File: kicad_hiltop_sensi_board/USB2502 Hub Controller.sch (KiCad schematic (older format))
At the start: 39 parts, among them U27 USB2502, U7 AT24C02C-SSHM-T, Y1 50ppm 24.000MHZ

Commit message: Updated LBBC board and Board layout started
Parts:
- JP14: footprint (none) -> Connector_PinHeader_1.00mm:PinHeader_1x02_P1.00mm_Vertical
- L1: footprint (none) -> Inductor_SMD:L_0805_2012Metric
- U7: footprint (none) -> Package_SO:SOIC-8_3.9x4.9mm_P1.27mm
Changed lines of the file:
@@
 F 0 "JP14" V 2696 8612 50  0000 R CNN
 F 1 "DNF" V 2605 8612 50  0000 R CNN
-F 2 "" H 2650 8700 50  0001 C CNN
+F 2 "Connector_PinHeader_1.00mm:PinHeader_1x02_P1.00mm_Vertical" H 2650 8700 50  0001 C CNN
 F 3 "" H 2650 8700 50  0001 C CNN
 	1    2650 8700
@@
 F 0 "L1" V 7500 8450 50  0000 C CNN
 F 1 "FB 500mA/0.10DCR" V 7600 8800 50  0000 C CNN
-F 2 "" V 7680 8700 50  0001 C CNN
+F 2 "Inductor_SMD:L_0805_2012Metric" V 7680 8700 50  0001 C CNN
 F 3 "" H 7750 8700 50  0001 C CNN
 	1    7750 8700
@@
 F 0 "U7" H 9375 6187 60  0000 C CNN
 F 1 "AT24C02C-SSHM-T" H 9375 6081 60  0000 C CNN
-F 2 "" H 9300 5150 60  0001 C CNN
+F 2 "Package_SO:SOIC-8_3.9x4.9mm_P1.27mm" H 9300 5150 60  0001 C CNN
 F 3 "" H 9300 5150 60  0001 C CNN
 	1    9350 5700

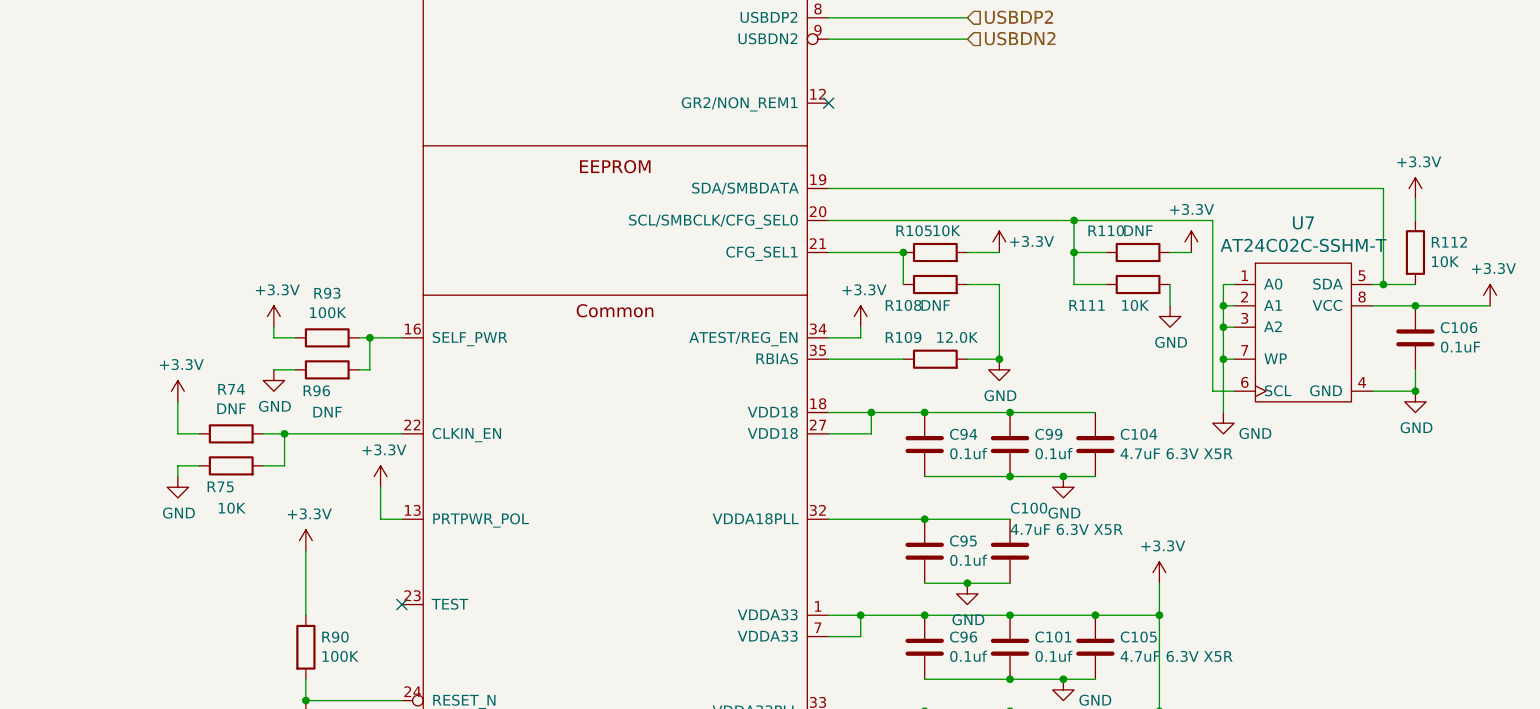
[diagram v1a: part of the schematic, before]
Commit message: Updated board layout LBBC sensi board
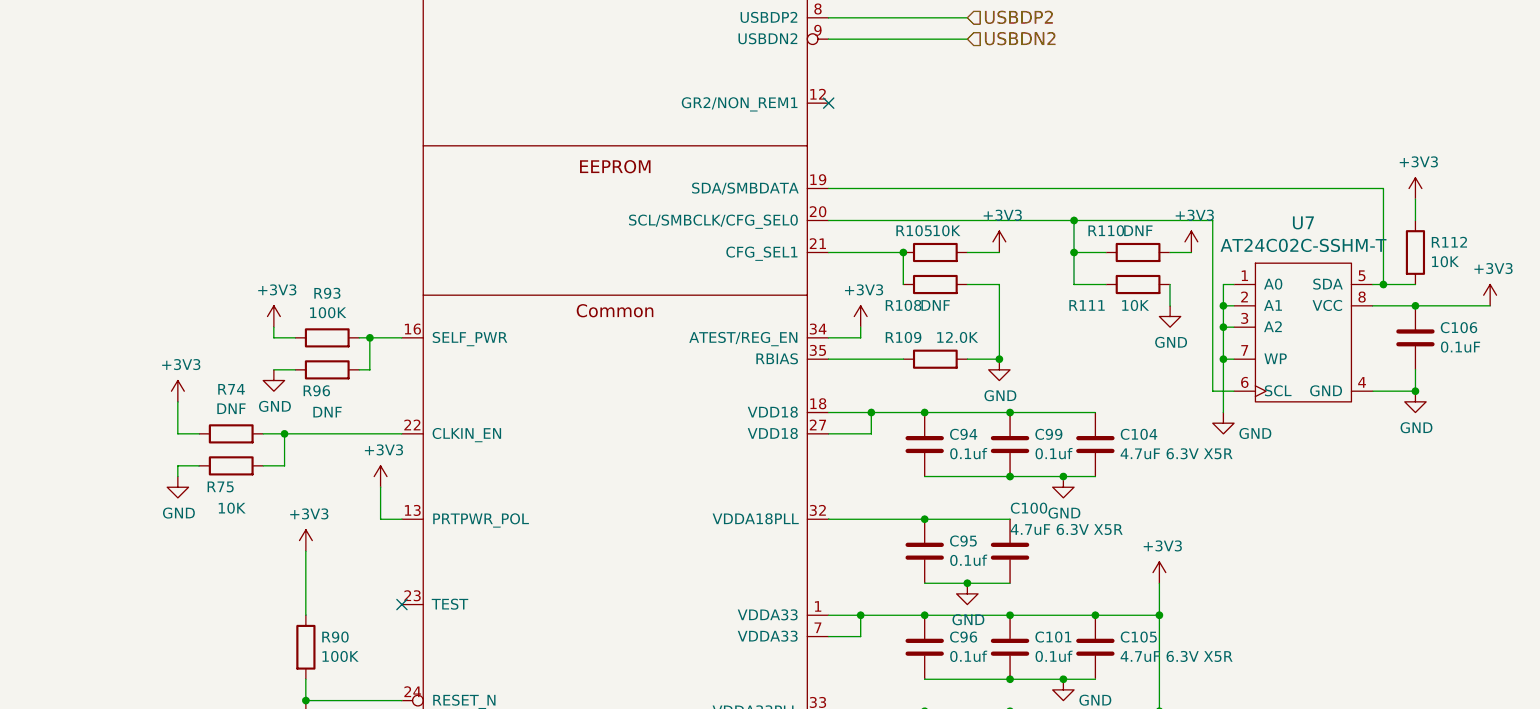
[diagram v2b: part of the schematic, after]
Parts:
- D1: footprint (none) -> Diode_SMD:D_SMA
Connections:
- net +5V_ISO1 renamed +3V3
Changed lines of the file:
@@
 Connection ~ 8000 7500
 Connection ~ 8400 7050
-$Comp
-L Devtank:+3.3V #PWR0178
-U 1 1 5D9260A5
-P 8700 6900
-F 0 "#PWR0178" H 8700 6750 50  0001 C CNN
-F 1 "+3.3V" H 8715 7073 50  0000 C CNN
-F 2 "" H 8700 6900 50  0000 C CNN
-F 3 "" H 8700 6900 50  0000 C CNN
-	1    8700 6900
-	1    0    0    -1
-$EndComp
 Wire Wire Line
 	8700 7050 8700 6900
@@
 	1    0    0    -1
 $EndComp
-$Comp
-L Devtank:+3.3V #PWR0201
-U 1 1 5D96A9AB
-P 7300 5700
-F 0 "#PWR0201" H 7300 5550 50  0001 C CNN
-F 1 "+3.3V" H 7315 5873 50  0000 C CNN
-F 2 "" H 7300 5700 50  0000 C CNN
-F 3 "" H 7300 5700 50  0000 C CNN
-	1    7300 5700
-	1    0    0    -1
-$EndComp
 Wire Wire Line
 	7300 5750 7300 5700
@@
 	7500 5500 7500 5350
 Connection ~ 7500 5350
-$Comp
-L Devtank:+3.3V #PWR0202
-U 1 1 5D97496E
-P 7950 5350
-F 0 "#PWR0202" H 7950 5200 50  0001 C CNN
-F 1 "+3.3V" H 8100 5400 50  0000 C CNN
-F 2 "" H 7950 5350 50  0000 C CNN
-F 3 "" H 7950 5350 50  0000 C CNN
-	1    7950 5350
-	1    0    0    -1
-$EndComp
 Wire Wire Line
 	7800 5350 7950 5350
@@
 	8300 5500 8300 5350
 Connection ~ 8300 5350
-$Comp
-L Devtank:+3.3V #PWR0205
-U 1 1 5D991A44
-P 8850 5350
-F 0 "#PWR0205" H 8850 5200 50  0001 C CNN
-F 1 "+3.3V" H 8850 5550 50  0000 C CNN
-F 2 "" H 8850 5350 50  0000 C CNN
-F 3 "" H 8850 5350 50  0000 C CNN
-	1    8850 5350
-	1    0    0    -1
-$EndComp
 Wire Wire Line
 	8750 5350 8850 5350
@@
 Wire Wire Line
 	9900 6000 9700 6000
-$Comp
-L Devtank:+3.3V #PWR0209
-U 1 1 5D9B0D62
-P 9900 5100
-F 0 "#PWR0209" H 9900 4950 50  0001 C CNN
-F 1 "+3.3V" H 9915 5273 50  0000 C CNN
-F 2 "" H 9900 5100 50  0000 C CNN
-F 3 "" H 9900 5100 50  0000 C CNN
-	1    9900 5100
-	1    0    0    -1
-$EndComp
 $Comp
 L device:R R112
@@
 Wire Wire Line
 	4700 7900 4700 7750
-$Comp
-L Devtank:+3.3V #PWR0211
-U 1 1 5DAA965D
-P 4700 6750
-F 0 "#PWR0211" H 4700 6600 50  0001 C CNN
-F 1 "+3.3V" H 4715 6923 50  0000 C CNN
-F 2 "" H 4700 6750 50  0000 C CNN
-F 3 "" H 4700 6750 50  0000 C CNN
-	1    4700 6750
-	1    0    0    -1
-$EndComp
 Wire Wire Line
 	4500 6200 4600 6200
@@
 	4600 6200 5150 6200
 Connection ~ 4600 6200
-$Comp
-L Devtank:+3.3V #PWR0212
-U 1 1 5DAE308D
-P 4100 6050
-F 0 "#PWR0212" H 4100 5900 50  0001 C CNN
-F 1 "+3.3V" H 4115 6223 50  0000 C CNN
-F 2 "" H 4100 6050 50  0000 C CNN
-F 3 "" H 4100 6050 50  0000 C CNN
-	1    4100 6050
-	1    0    0    -1
-$EndComp
 $Comp
 L power:GND #PWR0213
@@
 Wire Wire Line
 	4650 5900 4550 5900
-$Comp
-L Devtank:+3.3V #PWR0215
-U 1 1 5DB51EA9
-P 4550 5700
-F 0 "#PWR0215" H 4550 5550 50  0001 C CNN
-F 1 "+3.3V" H 4565 5873 50  0000 C CNN
-F 2 "" H 4550 5700 50  0000 C CNN
-F 3 "" H 4550 5700 50  0000 C CNN
-	1    4550 5700
-	1    0    0    -1
-$EndComp
 Wire Wire Line
 	4650 5750 4550 5750
@@
 Wire Wire Line
 	9900 5100 9900 5200
-$Comp
-L Devtank:+3.3V #PWR0223
-U 1 1 5DC7B6F6
-P 10250 5600
-F 0 "#PWR0223" H 10250 5450 50  0001 C CNN
-F 1 "+3.3V" H 10265 5773 50  0000 C CNN
-F 2 "" H 10250 5600 50  0000 C CNN
-F 3 "" H 10250 5600 50  0000 C CNN
-	1    10250 5600
-	1    0    0    -1
-$EndComp
 Wire Wire Line
 	9900 5600 10250 5600
@@
 F 0 "D1" H 4650 2266 50  0000 C CNN
 F 1 "B240A-13" H 4650 2175 50  0000 C CNN
-F 2 "" H 4650 2050 50  0001 C CNN
+F 2 "Diode_SMD:D_SMA" H 4650 2050 50  0001 C CNN
 F 3 "" H 4650 2050 50  0001 C CNN
 	1    4650 2050
@@
 Wire Wire Line
 	4700 6750 4700 7050
-$Comp
-L Devtank:+3.3V #PWR04
-U 1 1 5DC261DE
-P 5050 6450
-F 0 "#PWR04" H 5050 6300 50  0001 C CNN
-F 1 "+3.3V" H 5065 6623 50  0000 C CNN
-F 2 "" H 5050 6450 50  0000 C CNN
-F 3 "" H 5050 6450 50  0000 C CNN
-	1    5050 6450
-	1    0    0    -1
-$EndComp
 Wire Wire Line
 	5150 6600 5050 6600
@@
 	1    0    0    -1
 $EndComp
+$Comp
+L power:+3V3 #PWR?
+U 1 1 5E653672
+P 8700 6900
+AR Path="/5E653672" Ref="#PWR?"  Part="1"
+AR Path="/5D8D08E6/5E653672" Ref="#PWR0178"  Part="1"
+F 0 "#PWR0178" H 8700 6750 50  0001 C CNN
+F 1 "+3V3" H 8715 7073 50  0000 C CNN
+F 2 "" H 8700 6900 50  0001 C CNN
+F 3 "" H 8700 6900 50  0001 C CNN
+	1    8700 6900
+	1    0    0    -1
+$EndComp
+$Comp
+L power:+3V3 #PWR?
+U 1 1 5E664207
+P 7300 5700
+AR Path="/5E664207" Ref="#PWR?"  Part="1"
+AR Path="/5D8D08E6/5E664207" Ref="#PWR0201"  Part="1"
+F 0 "#PWR0201" H 7300 5550 50  0001 C CNN
+F 1 "+3V3" H 7315 5873 50  0000 C CNN
+F 2 "" H 7300 5700 50  0001 C CNN
+F 3 "" H 7300 5700 50  0001 C CNN
+	1    7300 5700
+	1    0    0    -1
+$EndComp
+$Comp
+L power:+3V3 #PWR?
+U 1 1 5E674F93
+P 7950 5350
+AR Path="/5E674F93" Ref="#PWR?"  Part="1"
+AR Path="/5D8D08E6/5E674F93" Ref="#PWR0202"  Part="1"
+F 0 "#PWR0202" H 7950 5200 50  0001 C CNN
+F 1 "+3V3" H 7965 5523 50  0000 C CNN
+F 2 "" H 7950 5350 50  0001 C CNN
+F 3 "" H 7950 5350 50  0001 C CNN
+	1    7950 5350
+	1    0    0    -1
+$EndComp
+$Comp
+L power:+3V3 #PWR?
+U 1 1 5E685BFA
+P 8850 5350
+AR Path="/5E685BFA" Ref="#PWR?"  Part="1"
+AR Path="/5D8D08E6/5E685BFA" Ref="#PWR0205"  Part="1"
+F 0 "#PWR0205" H 8850 5200 50  0001 C CNN
+F 1 "+3V3" H 8865 5523 50  0000 C CNN
+F 2 "" H 8850 5350 50  0001 C CNN
+F 3 "" H 8850 5350 50  0001 C CNN
+	1    8850 5350
+	1    0    0    -1
+$EndComp
+$Comp
+L power:+3V3 #PWR?
+U 1 1 5E693D22
+P 9900 5100
+AR Path="/5E693D22" Ref="#PWR?"  Part="1"
+AR Path="/5D8D08E6/5E693D22" Ref="#PWR0209"  Part="1"
+F 0 "#PWR0209" H 9900 4950 50  0001 C CNN
+F 1 "+3V3" H 9915 5273 50  0000 C CNN
+F 2 "" H 9900 5100 50  0001 C CNN
+F 3 "" H 9900 5100 50  0001 C CNN
+	1    9900 5100
+	1    0    0    -1
+$EndComp
+$Comp
+L power:+3V3 #PWR?
+U 1 1 5E6A7C04
+P 4700 6750
+AR Path="/5E6A7C04" Ref="#PWR?"  Part="1"
+AR Path="/5D8D08E6/5E6A7C04" Ref="#PWR0211"  Part="1"
+F 0 "#PWR0211" H 4700 6600 50  0001 C CNN
+F 1 "+3V3" H 4715 6923 50  0000 C CNN
+F 2 "" H 4700 6750 50  0001 C CNN
+F 3 "" H 4700 6750 50  0001 C CNN
+	1    4700 6750
+	1    0    0    -1
+$EndComp
+$Comp
+L power:+3V3 #PWR?
+U 1 1 5E6B8AFF
+P 5050 6450
+AR Path="/5E6B8AFF" Ref="#PWR?"  Part="1"
+AR Path="/5D8D08E6/5E6B8AFF" Ref="#PWR0212"  Part="1"
+F 0 "#PWR0212" H 5050 6300 50  0001 C CNN
+F 1 "+3V3" H 5065 6623 50  0000 C CNN
+F 2 "" H 5050 6450 50  0001 C CNN
+F 3 "" H 5050 6450 50  0001 C CNN
+	1    5050 6450
+	1    0    0    -1
+$EndComp
+$Comp
+L power:+3V3 #PWR?
+U 1 1 5E6C9168
+P 4100 6050
+AR Path="/5E6C9168" Ref="#PWR?"  Part="1"
+AR Path="/5D8D08E6/5E6C9168" Ref="#PWR0215"  Part="1"
+F 0 "#PWR0215" H 4100 5900 50  0001 C CNN
+F 1 "+3V3" H 4115 6223 50  0000 C CNN
+F 2 "" H 4100 6050 50  0001 C CNN
+F 3 "" H 4100 6050 50  0001 C CNN
+	1    4100 6050
+	1    0    0    -1
+$EndComp
+$Comp
+L power:+3V3 #PWR?
+U 1 1 5E6D7CDB
+P 4550 5700
+AR Path="/5E6D7CDB" Ref="#PWR?"  Part="1"
+AR Path="/5D8D08E6/5E6D7CDB" Ref="#PWR0223"  Part="1"
+F 0 "#PWR0223" H 4550 5550 50  0001 C CNN
+F 1 "+3V3" H 4565 5873 50  0000 C CNN
+F 2 "" H 4550 5700 50  0001 C CNN
+F 3 "" H 4550 5700 50  0001 C CNN
+	1    4550 5700
+	1    0    0    -1
+$EndComp
+$Comp
+L power:+3V3 #PWR?
+U 1 1 5E6E6DE1
+P 10250 5600
+AR Path="/5E6E6DE1" Ref="#PWR?"  Part="1"
+AR Path="/5D8D08E6/5E6E6DE1" Ref="#PWR0245"  Part="1"
+F 0 "#PWR0245" H 10250 5450 50  0001 C CNN
+F 1 "+3V3" H 10265 5773 50  0000 C CNN
+F 2 "" H 10250 5600 50  0001 C CNN
+F 3 "" H 10250 5600 50  0001 C CNN
+	1    10250 5600
+	1    0    0    -1
+$EndComp

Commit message: Updated sensi board layout LBBC
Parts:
- Y1: footprint (none) -> Crystal:Crystal_SMD_TXC_7A-2Pin_5x3.2mm
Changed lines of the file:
@@
 F 0 "Y1" V 4196 8419 50  0000 R CNN
 F 1 "50ppm 24.000MHZ" V 4000 8800 50  0000 R CNN
-F 2 "" H 4150 8550 50  0001 C CNN
+F 2 "Crystal:Crystal_SMD_TXC_7A-2Pin_5x3.2mm" H 4150 8550 50  0001 C CNN
 F 3 "" H 4150 8550 50  0001 C CNN
 	1    4150 8550

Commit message: Sensi board updated pin map
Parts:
- C101, C106, C92, C93, C94, C95, C96, C97, C98, C99: footprint Capacitor_SMD:C_0603_1608Metric -> Capacitor_SMD:C_0402_1005Metric
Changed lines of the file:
@@
 F 0 "C101" H 8115 7246 50  0000 L CNN
 F 1 "0.1uf" H 8115 7155 50  0000 L CNN
-F 2 "Capacitor_SMD:C_0603_1608Metric" H 8038 7050 50  0001 C CNN
+F 2 "Capacitor_SMD:C_0402_1005Metric" H 8038 7050 50  0001 C CNN
 F 3 "" H 8000 7200 50  0001 C CNN
 	1    8000 7200
@@
 F 0 "C96" H 7715 7246 50  0000 L CNN
 F 1 "0.1uf" H 7715 7155 50  0000 L CNN
-F 2 "Capacitor_SMD:C_0603_1608Metric" H 7638 7050 50  0001 C CNN
+F 2 "Capacitor_SMD:C_0402_1005Metric" H 7638 7050 50  0001 C CNN
 F 3 "" H 7600 7200 50  0001 C CNN
 	1    7600 7200
@@
 F 0 "C97" H 7715 7696 50  0000 L CNN
 F 1 "0.1uf" H 7715 7605 50  0000 L CNN
-F 2 "Capacitor_SMD:C_0603_1608Metric" H 7638 7500 50  0001 C CNN
+F 2 "Capacitor_SMD:C_0402_1005Metric" H 7638 7500 50  0001 C CNN
 F 3 "" H 7600 7650 50  0001 C CNN
 	1    7600 7650
@@
 F 0 "C95" H 7715 6796 50  0000 L CNN
 F 1 "0.1uf" H 7715 6705 50  0000 L CNN
-F 2 "Capacitor_SMD:C_0603_1608Metric" H 7638 6600 50  0001 C CNN
+F 2 "Capacitor_SMD:C_0402_1005Metric" H 7638 6600 50  0001 C CNN
 F 3 "" H 7600 6750 50  0001 C CNN
 	1    7600 6750
@@
 F 0 "C99" H 8115 6296 50  0000 L CNN
 F 1 "0.1uf" H 8115 6205 50  0000 L CNN
-F 2 "Capacitor_SMD:C_0603_1608Metric" H 8038 6100 50  0001 C CNN
+F 2 "Capacitor_SMD:C_0402_1005Metric" H 8038 6100 50  0001 C CNN
 F 3 "" H 8000 6250 50  0001 C CNN
 	1    8000 6250
@@
 F 0 "C94" H 7715 6296 50  0000 L CNN
 F 1 "0.1uf" H 7715 6205 50  0000 L CNN
-F 2 "Capacitor_SMD:C_0603_1608Metric" H 7638 6100 50  0001 C CNN
+F 2 "Capacitor_SMD:C_0402_1005Metric" H 7638 6100 50  0001 C CNN
 F 3 "" H 7600 6250 50  0001 C CNN
 	1    7600 6250
@@
 F 0 "C106" H 10015 5796 50  0000 L CNN
 F 1 "0.1uF" H 10015 5705 50  0000 L CNN
-F 2 "Capacitor_SMD:C_0603_1608Metric" H 9938 5600 50  0001 C CNN
+F 2 "Capacitor_SMD:C_0402_1005Metric" H 9938 5600 50  0001 C CNN
 F 3 "" H 9900 5750 50  0001 C CNN
 	1    9900 5750
@@
 F 0 "C98" H 7715 8146 50  0000 L CNN
 F 1 "0.1uf" H 7715 8055 50  0000 L CNN
-F 2 "Capacitor_SMD:C_0603_1608Metric" H 7638 7950 50  0001 C CNN
+F 2 "Capacitor_SMD:C_0402_1005Metric" H 7638 7950 50  0001 C CNN
 F 3 "" H 7600 8100 50  0001 C CNN
 	1    7600 8100
@@
 F 0 "C92" H 5500 2550 50  0000 L CNN
 F 1 "0.1uF" H 5500 2450 50  0000 L CNN
-F 2 "Capacitor_SMD:C_0603_1608Metric" H 5588 2050 50  0001 C CNN
+F 2 "Capacitor_SMD:C_0402_1005Metric" H 5588 2050 50  0001 C CNN
 F 3 "" H 5550 2200 50  0001 C CNN
 	1    5550 2200
@@
 F 0 "C93" H 5965 2246 50  0000 L CNN
 F 1 "0.1uF" H 5965 2155 50  0000 L CNN
-F 2 "Capacitor_SMD:C_0603_1608Metric" H 5888 2050 50  0001 C CNN
+F 2 "Capacitor_SMD:C_0402_1005Metric" H 5888 2050 50  0001 C CNN
 F 3 "" H 5850 2200 50  0001 C CNN
 	1    5850 2200
